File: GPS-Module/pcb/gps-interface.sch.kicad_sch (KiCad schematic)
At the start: 3 parts, among them U1 MAX-8C

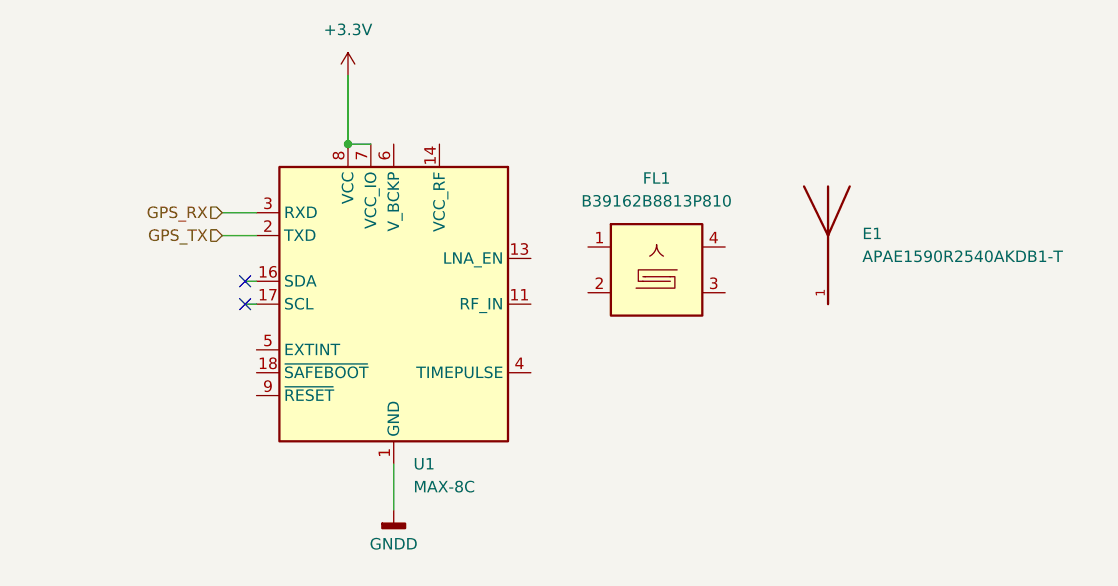
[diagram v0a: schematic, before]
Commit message: Added footprints for GPS module, new edge cuts for main module
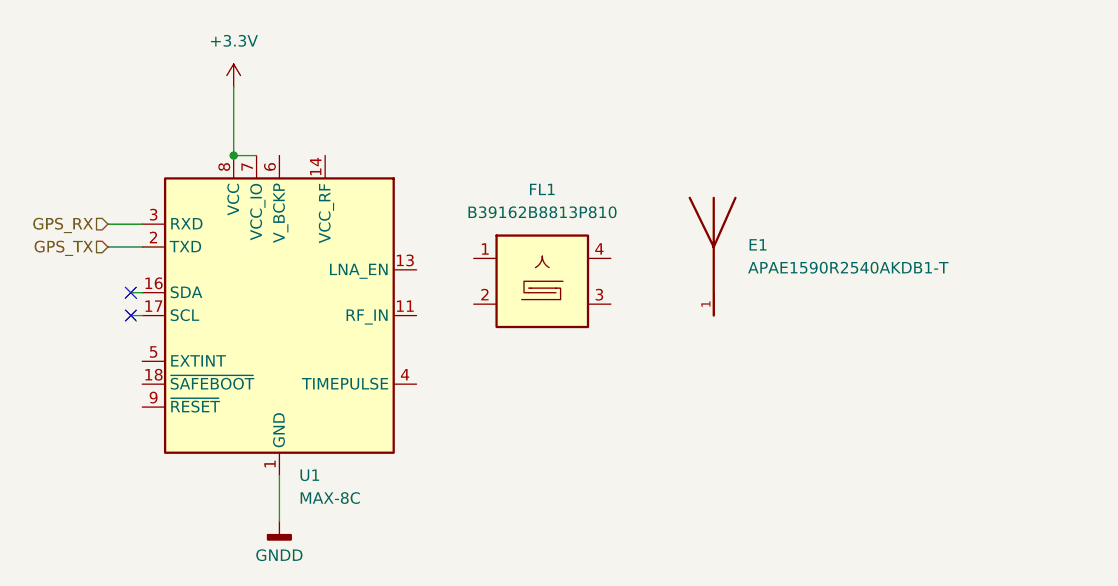
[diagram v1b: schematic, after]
